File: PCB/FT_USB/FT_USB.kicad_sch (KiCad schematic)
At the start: 2 parts, among them CON1 USB_B, CON2 Conn_01x03

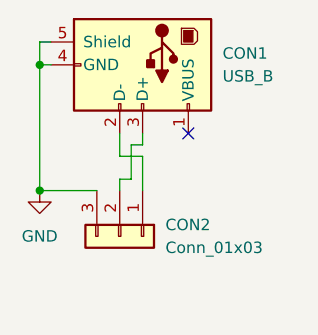
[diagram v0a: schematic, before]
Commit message: .gitignore update, USB update
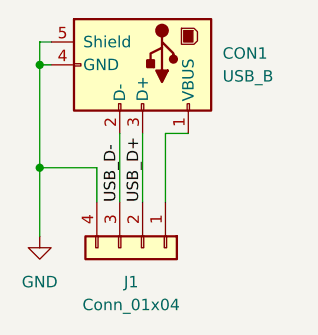
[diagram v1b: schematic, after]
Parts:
- removed CON2: Conn_01x03, Connector_PinHeader_2.54mm:PinHeader_1x03_P2.54mm_Vertical, symbol Connector_Generic:Conn_01x03
- added J1: Conn_01x04, Connector_PinHeader_2.54mm:PinHeader_1x04_P2.54mm_Vertical, symbol Connector_Generic:Conn_01x04
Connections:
- net GND: now also J1.4 (Pin_4)
- net USB_D-: now reaches CON1.2 (D-)
- net USB_D-: now also J1.3 (Pin_3)
- net USB_D+: now reaches CON1.3 (D+)
- net USB_D+: now also J1.2 (Pin_2)
- net at CON1.1 (VBUS): now also J1.1 (Pin_1)
- no-connect marks 1 -> 0
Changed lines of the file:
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@@
 	(paper "A4")
-	(junction
-		(at 90.17 90.17)
-		(diameter 0)
-		(color 0 0 0 0)
-	)
 	(junction
 		(at 90.17 76.2)
@@
 		(color 0 0 0 0)
 	)
-	(no_connect
-		(at 106.68 83.82)
-	)
-	(wire
-		(pts
-			(xy 101.6 83.82) (xy 101.6 85.09)
-		)
-		(stroke
-			(width 0)
-			(type default)
-		)
-	)
-	(wire
-		(pts
-			(xy 99.06 86.36) (xy 101.6 86.36)
-		)
-		(stroke
-			(width 0)
-			(type default)
-		)
-	)
-	(wire
-		(pts
-			(xy 99.06 88.9) (xy 99.06 90.17)
-		)
-		(stroke
-			(width 0)
-			(type default)
-		)
-	)
-	(wire
-		(pts
-			(xy 101.6 86.36) (xy 101.6 90.17)
-		)
-		(stroke
-			(width 0)
-			(type default)
-		)
-	)
-	(wire
-		(pts
-			(xy 101.6 85.09) (xy 100.33 85.09)
-		)
-		(stroke
-			(width 0)
-			(type default)
-		)
-	)
-	(wire
-		(pts
-			(xy 90.17 76.2) (xy 90.17 90.17)
+	(junction
+		(at 90.17 87.63)
+		(diameter 0)
+		(color 0 0 0 0)
+	)
+	(wire
+		(pts
+			(xy 101.6 83.82) (xy 101.6 91.44)
+		)
+		(stroke
+			(width 0)
+			(type default)
+		)
+	)
+	(wire
+		(pts
+			(xy 90.17 87.63) (xy 90.17 95.25)
+		)
+		(stroke
+			(width 0)
+			(type default)
+		)
+	)
+	(wire
+		(pts
+			(xy 90.17 76.2) (xy 90.17 87.63)
 		)
 		(stroke
@@
 	(wire
 		(pts
-			(xy 99.06 83.82) (xy 99.06 86.36)
-		)
-		(stroke
-			(width 0)
-			(type default)
-		)
-	)
-	(wire
-		(pts
-			(xy 90.17 90.17) (xy 96.52 90.17)
-		)
-		(stroke
-			(width 0)
-			(type default)
-		)
-	)
-	(wire
-		(pts
-			(xy 100.33 88.9) (xy 99.06 88.9)
+			(xy 96.52 87.63) (xy 96.52 91.44)
+		)
+		(stroke
+			(width 0)
+			(type default)
+		)
+	)
+	(wire
+		(pts
+			(xy 104.14 91.44) (xy 104.14 83.82)
+		)
+		(stroke
+			(width 0)
+			(type default)
+		)
+	)
+	(wire
+		(pts
+			(xy 90.17 87.63) (xy 96.52 87.63)
+		)
+		(stroke
+			(width 0)
+			(type default)
+		)
+	)
+	(wire
+		(pts
+			(xy 99.06 83.82) (xy 99.06 91.44)
 		)
 		(stroke
@@
 	(wire
 		(pts
-			(xy 100.33 85.09) (xy 100.33 88.9)
-		)
-		(stroke
-			(width 0)
-			(type default)
+			(xy 104.14 83.82) (xy 106.68 83.82)
+		)
+		(stroke
+			(width 0)
+			(type default)
+		)
+	)
+	(label "USB_D-"
+		(at 99.06 91.44 90)
+		(fields_autoplaced yes)
+		(effects
+			(font
+				(size 1.27 1.27)
+			)
+			(justify left bottom)
+		)
+	)
+	(label "USB_D+"
+		(at 101.6 91.44 90)
+		(fields_autoplaced yes)
+		(effects
+			(font
+				(size 1.27 1.27)
+			)
+			(justify left bottom)
 		)
 	)
 	(symbol
 		(lib_id "power:GND")
-		(at 90.17 90.17 0)
+		(at 90.17 95.25 0)
 		(unit 1)
 		(exclude_from_sim no)
@@
 		(fields_autoplaced yes)
 		(property "Reference" "#PWR01"
-			(at 90.17 96.52 0)
+			(at 90.17 101.6 0)
 			(effects
 				(font
@@
 		)
 		(property "Value" "GND"
+			(at 90.17 100.33 0)
+			(effects
+				(font
+					(size 1.27 1.27)
+				)
+			)
+		)
+		(property "Footprint" ""
 			(at 90.17 95.25 0)
 			(effects
@@
 					(size 1.27 1.27)
 				)
-			)
-		)
-		(property "Footprint" ""
-			(at 90.17 90.17 0)
-			(effects
-				(font
-					(size 1.27 1.27)
-				)
 				(hide yes)
 			)
 		)
 		(property "Datasheet" ""
-			(at 90.17 90.17 0)
+			(at 90.17 95.25 0)
 			(effects
 				(font
@@
 		)
 		(property "Description" "Power symbol creates a global label with name \"GND\" , ground"
-			(at 90.17 90.17 0)
+			(at 90.17 95.25 0)
 			(effects
 				(font
@@
 				(path "/23b06d04-94b1-4b12-b68f-9e0b5d3168f9"
 					(reference "#PWR01")
-					(unit 1)
-				)
-			)
-		)
-	)
-	(symbol
-		(lib_id "Connector_Generic:Conn_01x03")
-		(at 99.06 95.25 270)
-		(unit 1)
-		(exclude_from_sim no)
-		(in_bom yes)
-		(on_board yes)
-		(dnp no)
-		(fields_autoplaced yes)
-		(property "Reference" "CON2"
-			(at 104.14 93.9799 90)
-			(effects
-				(font
-					(size 1.27 1.27)
-				)
-				(justify left)
-			)
-		)
-		(property "Value" "Conn_01x03"
-			(at 104.14 96.5199 90)
-			(effects
-				(font
-					(size 1.27 1.27)
-				)
-				(justify left)
-			)
-		)
-		(property "Footprint" "Connector_PinHeader_2.54mm:PinHeader_1x03_P2.54mm_Vertical"
-			(at 99.06 95.25 0)
-			(effects
-				(font
-					(size 1.27 1.27)
-				)
-				(hide yes)
-			)
-		)
-		(property "Datasheet" "https://img.gme.cz/files/eshop_data/eshop_data/5/800-164/dsh.800-164.1.pdf"
-			(at 99.06 95.25 0)
-			(effects
-				(font
-					(size 1.27 1.27)
-				)
-				(hide yes)
-			)
-		)
-		(property "Description" "Generic connector, single row, 01x03, script generated (kicad-library-utils/schlib/autogen/connector/)"
-			(at 99.06 95.25 0)
-			(effects
-				(font
-					(size 1.27 1.27)
-				)
-				(hide yes)
-			)
-		)
-		(property "Assemble" "NO"
-			(at 99.06 95.25 0)
-			(effects
-				(font
-					(size 1.27 1.27)
-				)
-				(hide yes)
-			)
-		)
-		(property "Supplier" "GME"
-			(at 99.06 95.25 0)
-			(effects
-				(font
-					(size 1.27 1.27)
-				)
-				(hide yes)
-			)
-		)
-		(property "Supplier no." "800-164"
-			(at 99.06 95.25 0)
-			(effects
-				(font
-					(size 1.27 1.27)
-				)
-				(hide yes)
-			)
-		)
-		(property "URL" "https://www.gme.cz/v/1497964/kls-psh02-03pg-konektor-vidlice-roztec-254mm-1x3piny-prima-do-dps"
-			(at 99.06 95.25 0)
-			(effects
-				(font
-					(size 1.27 1.27)
-				)
-				(hide yes)
-			)
-		)
-		(pin "1"
-		)
-		(pin "3"
-		)
-		(pin "2"
-		)
-		(instances
-			(project "FT_USB"
-				(path "/23b06d04-94b1-4b12-b68f-9e0b5d3168f9"
-					(reference "CON2")
 					(unit 1)
 				)
@@
 			)
 		)
+		(property "Accept alternative part" "~"
+			(at 101.6 76.2 0)
+			(effects
+				(font
+					(size 1.27 1.27)
+				)
+				(hide yes)
+			)
+		)
 		(pin "3"
 		)
@@
 					(unit 1)
 				)
+			)
+		)
+	)
+	(symbol
+		(lib_id "Connector_Generic:Conn_01x04")
+		(at 101.6 96.52 270)
+		(unit 1)
+		(exclude_from_sim no)
+		(in_bom yes)
+		(on_board yes)
+		(dnp no)
+		(fields_autoplaced yes)
+		(property "Reference" "J1"
+			(at 100.33 100.33 90)
+			(effects
+				(font
+					(size 1.27 1.27)
+				)
+			)
+		)
+		(property "Value" "Conn_01x04"
+			(at 100.33 102.87 90)
+			(effects
+				(font
+					(size 1.27 1.27)
+				)
+			)
+		)
+		(property "Footprint" "Connector_PinHeader_2.54mm:PinHeader_1x04_P2.54mm_Vertical"
+			(at 101.6 96.52 0)
+			(effects
+				(font
+					(size 1.27 1.27)
+				)
+				(hide yes)
+			)
+		)
+		(property "Datasheet" "https://img.gme.cz/files/eshop_data/eshop_data/5/800-170/dsh.800-170.1.pdf"
+			(at 101.6 96.52 0)
+			(effects
+				(font
+					(size 1.27 1.27)
+				)
+				(hide yes)
+			)
+		)
+		(property "Description" "Generic connector, single row, 01x04, script generated (kicad-library-utils/schlib/autogen/connector/)"
+			(at 101.6 96.52 0)
+			(effects
+				(font
+					(size 1.27 1.27)
+				)
+				(hide yes)
+			)
+		)
+		(property "Accept alternative part" "~"
+			(at 101.6 96.52 0)
+			(effects
+				(font
+					(size 1.27 1.27)
+				)
+				(hide yes)
+			)
+		)
+		(property "Assemble" "NO"
+			(at 101.6 96.52 0)
+			(effects
+				(font
+					(size 1.27 1.27)
+				)
+				(hide yes)
+			)
+		)
+		(property "Supplier" "GME"
+			(at 101.6 96.52 0)
+			(effects
+				(font
+					(size 1.27 1.27)
+				)
+				(hide yes)
+			)
+		)
+		(property "Supplier no." "800-170"
+			(at 101.6 96.52 0)
+			(effects
+				(font
+					(size 1.27 1.27)
+				)
+				(hide yes)
+			)
+		)
+		(property "URL" "https://www.gme.cz/v/1497969/kls-psh02-04pg-konektor-vidlice-roztec-254mm-1x4piny-prima-do-dps"
+			(at 101.6 96.52 0)
+			(effects
+				(font
+					(size 1.27 1.27)
+				)
+				(hide yes)
+			)
+		)
+		(pin "1"
+		)
+		(pin "3"
+		)
+		(pin "4"
+		)
+		(pin "2"
+		)
+		(instances
+			(project "FT_USB"
+				(path "/23b06d04-94b1-4b12-b68f-9e0b5d3168f9"
+					(reference "J1")
+					(unit 1)
+				)

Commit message: panelization
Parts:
- renumbered CON1 to CON301, J1 to CON302
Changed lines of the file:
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@@
 		(dnp no)
 		(fields_autoplaced yes)
-		(property "Reference" "CON1"
+		(property "Reference" "CON301"
 			(at 110.49 74.9299 90)
 			(effects
@@
 			(project "FT_USB"
 				(path "/23b06d04-94b1-4b12-b68f-9e0b5d3168f9"
-					(reference "CON1")
+					(reference "CON301")
 					(unit 1)
 				)
@@
 		(dnp no)
 		(fields_autoplaced yes)
-		(property "Reference" "J1"
+		(property "Reference" "CON302"
 			(at 100.33 100.33 90)
 			(effects
@@
 			(project "FT_USB"
 				(path "/23b06d04-94b1-4b12-b68f-9e0b5d3168f9"
-					(reference "J1")
+					(reference "CON302")
 					(unit 1)
 				)
